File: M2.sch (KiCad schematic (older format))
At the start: 1 part

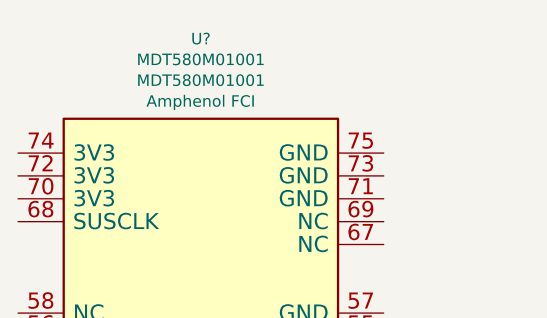
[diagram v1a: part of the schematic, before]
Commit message: added components to pcb and fixed corresponding errors
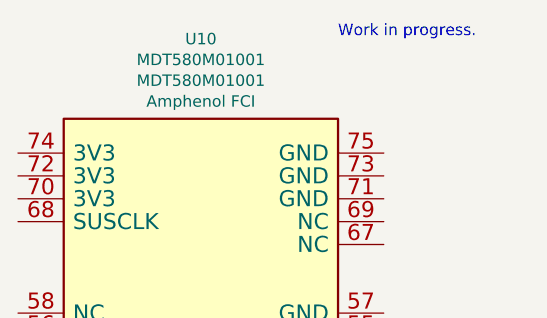
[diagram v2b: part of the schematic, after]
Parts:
- gave numbers to parts that had none: 1
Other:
- note added: "Work in progress."
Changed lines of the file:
@@
 $Descr A4 11693 8268
 encoding utf-8
-Sheet 10 10
+Sheet 9 10
 Title ""
 Date ""
@@
 $EndDescr
 $Comp
-L antmicroPciConnectors:MDT580M01001 U?
+L antmicroPciConnectors:MDT580M01001 U10
 U 1 1 61A7DEAD
 P 4100 4100
-F 0 "U?" H 4100 6849 50  0000 C CNN
+F 0 "U10" H 4100 6849 50  0000 C CNN
 F 1 "MDT580M01001" H 4100 6758 50  0000 C CNN
 F 2 "antmicro-footprints:MDT580M01001" H 4100 4100 50  0001 C CNN
@@
 	1    0    0    -1
 $EndComp
+Text Notes 4700 1350 0    50   ~ 0
+Work in progress.
 $EndSCHEMATC

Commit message: annotations
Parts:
- renumbered U10 to U12
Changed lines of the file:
@@
 $EndDescr
 $Comp
-L antmicroPciConnectors:MDT580M01001 U10
+L antmicroPciConnectors:MDT580M01001 U12
 U 1 1 61A7DEAD
 P 4100 4100
-F 0 "U10" H 4100 6849 50  0000 C CNN
+F 0 "U12" H 4100 6849 50  0000 C CNN
 F 1 "MDT580M01001" H 4100 6758 50  0000 C CNN
 F 2 "antmicro-footprints:MDT580M01001" H 4100 4100 50  0001 C CNN

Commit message: Add local libs to fix CI
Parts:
- U12: footprint antmicro-footprints:MDT580M01001 -> sa800u-baseboard-hw-footprints:MDT580M01001; symbol antmicroPciConnectors:MDT580M01001 -> sa800u-baseboard-hw:MDT580M01001
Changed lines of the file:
@@
 $EndDescr
 $Comp
-L antmicroPciConnectors:MDT580M01001 U12
+L sa800u-baseboard-hw:MDT580M01001 U12
 U 1 1 61A7DEAD
 P 4100 4100
 F 0 "U12" H 4100 6849 50  0000 C CNN
 F 1 "MDT580M01001" H 4100 6758 50  0000 C CNN
-F 2 "antmicro-footprints:MDT580M01001" H 4100 4100 50  0001 C CNN
+F 2 "sa800u-baseboard-hw-footprints:MDT580M01001" H 4100 4100 50  0001 C CNN
 F 3 "" H 4100 4100 50  0001 C CNN
 F 4 "MDT580M01001" H 4100 6667 50  0000 C CNN "MPN"
